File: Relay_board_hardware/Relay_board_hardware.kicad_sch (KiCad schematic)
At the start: 15 parts, among them IC1 BTS3800SL, Q1 IRF740ASPBF, U1 MCP6497T-E/SN

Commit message: bom updated with prices
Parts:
- C1: Price (none) -> 0.46
- Conn1: Price (none) -> 1.84
- IC1: Price (none) -> 0.95
- K1, K2: Price (none) -> 38.77
- Q1: Price (none) -> 2.28
- R1: Price (none) -> 0.37
- R2: Price (none) -> 0.38
- U1: Price (none) -> 0.76
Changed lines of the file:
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@@
       (effects (font (size 1.524 1.524)) hide)
+    )
+    (property "Price" "" (at 33.655 110.49 0)
+      (effects (font (size 1.27 1.27)) hide)
     )
     (pin "1")
@@
     )
     (property "Datasheet" "https://www.mouser.com/ProductDetail/Microchip-Technology/MCP6497T-E-SN?qs=8Wlm6%252BaMh8Sq3ZIB9JIi0Q%3D%3D" (at 171.45 101.6 0)
+      (effects (font (size 1.27 1.27)) hide)
+    )
+    (property "Price" "0.76" (at 171.45 101.6 0)
       (effects (font (size 1.27 1.27)) hide)
     )
@@
       (effects (font (size 1.27 1.27)) hide)
     )
+    (property "Price" "0.46" (at 104.14 119.38 0)
+      (effects (font (size 1.27 1.27)) hide)
+    )
     (pin "1")
     (pin "2")
@@
       (effects (font (size 1.524 1.524)) hide)
     )
+    (property "Price" "" (at 222.25 87.63 0)
+      (effects (font (size 1.27 1.27)) hide)
+    )
     (pin "1")
     (pin "2")
@@
       (effects (font (size 1.27 1.27)) (justify left top) hide)
     )
+    (property "Price" "0.95" (at 76.2 74.93 0)
+      (effects (font (size 1.27 1.27)) hide)
+    )
     (pin "1")
     (pin "2")
@@
       (effects (font (size 1.524 1.524)) hide)
     )
-    (property "Datasheet" "" (at 20.32 90.17 0)
-      (effects (font (size 1.524 1.524)) hide)
+    (property "Datasheet" "https://powerwerx.com/anderson-powerpole-colored-housings" (at 20.32 90.17 0)
+      (effects (font (size 1.524 1.524)) hide)
+    )
+    (property "Price" "1.84" (at 24.13 76.2 0)
+      (effects (font (size 1.27 1.27)) hide)
     )
     (pin "1")
@@
       (effects (font (size 1.27 1.27)) hide)
     )
+    (property "Price" "38.77" (at 59.69 59.69 0)
+      (effects (font (size 1.27 1.27)) hide)
+    )
     (pin "1")
     (pin "2")
@@
     )
     (property "Datasheet" "https://www.mouser.com/ProductDetail/Microchip-Technology/MCP6497T-E-SN?qs=8Wlm6%252BaMh8Sq3ZIB9JIi0Q%3D%3D" (at 171.45 78.74 0)
+      (effects (font (size 1.27 1.27)) hide)
+    )
+    (property "Price" "0.76" (at 171.45 78.74 0)
       (effects (font (size 1.27 1.27)) hide)
     )
@@
       (effects (font (size 1.524 1.524)) hide)
     )
+    (property "Price" "" (at 54.61 110.49 0)
+      (effects (font (size 1.27 1.27)) hide)
+    )
     (pin "1")
     (instances
@@
     )
     (property "Datasheet" "https://www.mouser.com/ProductDetail/Vishay-Semiconductors/IRF740ASPBF?qs=I1ZA2VTqfvSWXSCbb2jmeg%3D%3D" (at 121.92 92.71 0)
+      (effects (font (size 1.27 1.27)) hide)
+    )
+    (property "Price" "2.28" (at 121.92 92.71 0)
       (effects (font (size 1.27 1.27)) hide)
     )
@@
       (effects (font (size 1.524 1.524)) hide)
     )
+    (property "Price" "" (at 124.46 80.01 0)
+      (effects (font (size 1.27 1.27)) hide)
+    )
     (pin "1")
     (instances
@@
       (effects (font (size 1.27 1.27)) hide)
     )
+    (property "Price" "0.38" (at 151.13 81.28 0)
+      (effects (font (size 1.27 1.27)) hide)
+    )
     (pin "1")
     (pin "2")
@@
     )
     (property "Datasheet" "https://www.mouser.com/ProductDetail/Panasonic-Industrial-Devices/AECN11012?qs=vmHwEFxEFR%2FxpGCT4n%2FbmQ%3D%3D" (at 59.69 65.405 0)
+      (effects (font (size 1.27 1.27)) hide)
+    )
+    (property "Price" "38.77" (at 59.69 92.71 0)
       (effects (font (size 1.27 1.27)) hide)
     )
@@
       (effects (font (size 1.524 1.524)) hide)
     )
+    (property "Price" "" (at 29.21 46.99 0)
+      (effects (font (size 1.27 1.27)) hide)
+    )
     (pin "1")
     (instances
@@
       (effects (font (size 1.524 1.524)) hide)
     )
-    (property "Datasheet" "" (at 20.32 95.25 0)
-      (effects (font (size 1.524 1.524)) hide)
+    (property "Datasheet" "https://powerwerx.com/anderson-powerpole-colored-housings" (at 20.32 95.25 0)
+      (effects (font (size 1.524 1.524)) hide)
+    )
+    (property "Price" "1.84" (at 24.13 81.28 0)
+      (effects (font (size 1.27 1.27)) hide)
     )
     (pin "1")
@@
     )
     (property "Datasheet" "https://www.mouser.com/ProductDetail/Vishay-Dale/CRCW2512649KFKEG?qs=WpL82mpZNv9YmPWivNEPLA%3D%3D" (at 151.13 71.12 0)
+      (effects (font (size 1.27 1.27)) hide)
+    )
+    (property "Price" "0.37" (at 151.13 71.12 0)
       (effects (font (size 1.27 1.27)) hide)
     )
@@
       (effects (font (size 1.524 1.524)) hide)
     )
-    (pin "1")
+    (property "Price" "" (at 52.07 46.99 0)
+      (effects (font (size 1.27 1.27)) hide)
+    )
+    (pin "1")

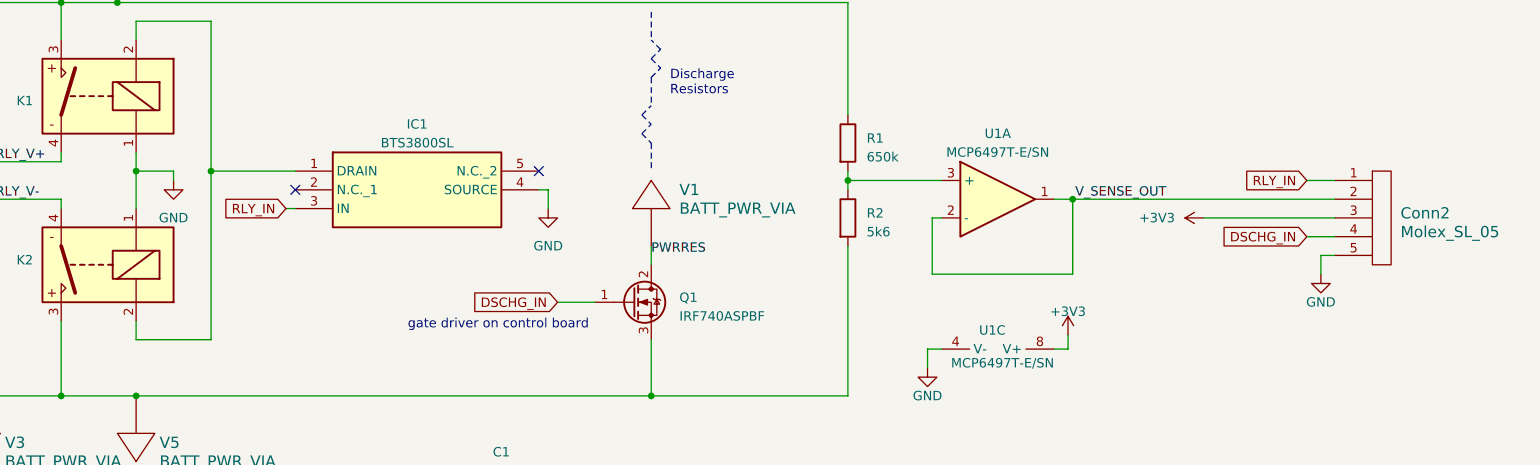
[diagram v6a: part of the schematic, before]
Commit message: 12V connection redesign
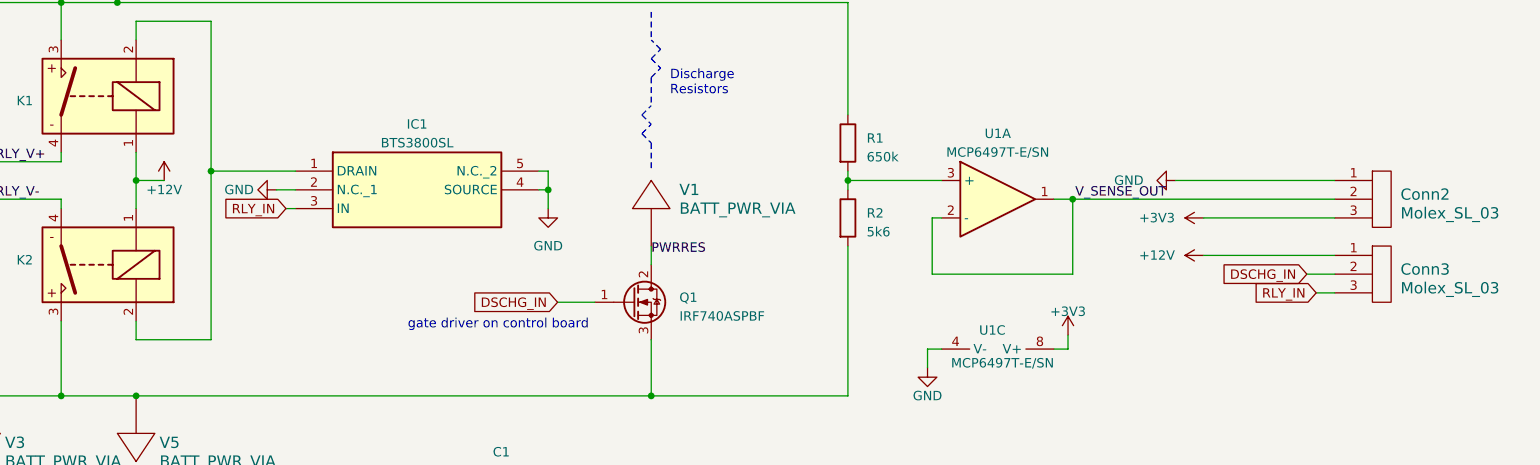
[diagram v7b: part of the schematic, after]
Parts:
- removed Conn2: Molex_SL_05, 0-customs:MOLEX_SL_05_Horizontal, symbol 0-customs:Molex_SL_05
- added Conn2, Conn3: Molex_SL_03, 0-customs:MOLEX_SL_03_Horizontal, symbol 0-customs:Molex_SL_03
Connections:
- net +3V3: now also Conn2.3
- net DSCHG_IN: now also Conn3.2
- net GND: now also IC1.2 (N.C._1), IC1.5 (N.C._2), Conn2.1; no longer K1.1, K2.1
- net RLY_IN: now also Conn3.3
- net V_SENSE_OUT: now also Conn2.2
- new net +12V: Conn3.1, K1.1, K2.1
- no-connect marks 2 -> 0

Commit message: R2 edits
gerbs generated
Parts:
- added R3: 10k, Resistor_SMD:R_0603_1608Metric_Pad0.98x0.95mm_HandSolder, symbol Device:R
- added U2: MCP1416, Package_TO_SOT_SMD:SOT-23-5, symbol Driver_FET:MCP1416
- C1: value 4.7n -> 1u; footprint Capacitor_THT:C_Rect_L13.0mm_W5.0mm_P10.00mm_FKS3_FKP3_MKS4 -> Capacitor_SMD:C_0603_1608Metric_Pad1.08x0.95mm_HandSolder; Price 0.46 -> (none)
- U1: value MCP6497T-E/SN -> AD8541
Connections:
- net +12V: now also C1.1, U2.2 (Vdd)
- net +3V3: now also U1.7 (V+); no longer U1.8 (V+)
- net DSCHG_IN: now also U2.3 (IN); no longer Q1.1 (G)
- net GND: now also K2.3, Q1.3 (S), R2.2, V3.1, V5.1, R3.1, U2.1 (NC), U2.4 (GND)
- net V_SENSE_OUT: now also U1.6; no longer U1.1
- removed net GNDPWR: C1.1, K2.3, Q1.3 (S), R2.2, V3.1, V5.1
- new net: Q1.1 (G), R3.2, U2.5 (OUT)
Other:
- note removed: "Y-rated capacitor"
- note removed: "gate driver on control board"
- moved on the sheet: Conn1A, Conn1B, Conn2, Conn3, IC1, K1, K2, Q1, R1, R2, U1A, V1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
